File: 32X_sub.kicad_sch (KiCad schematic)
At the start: 103 parts, among them IC511 315-5684, IC512 315-5788, IC515 74HC74, IC516 74LS00, T520 TestPoint, T526 TestPoint, T527 TestPoint, T528 TestPoint, T547 TestPoint, T548 TestPoint, T555 TestPoint, T599 AS, X501 *3

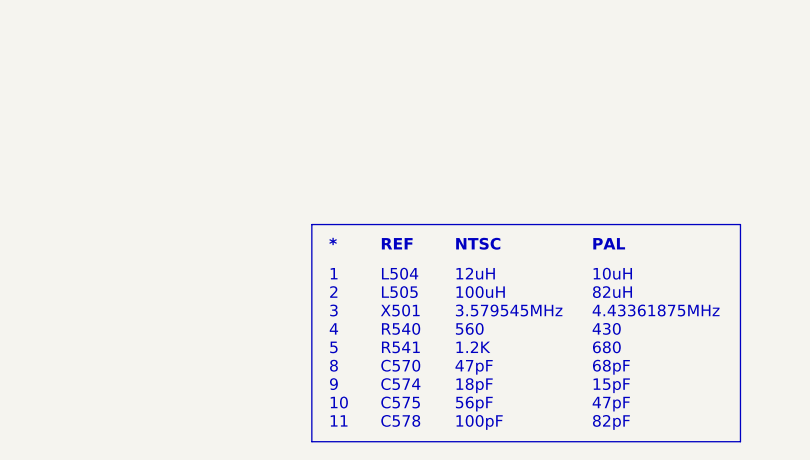
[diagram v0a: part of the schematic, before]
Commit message: Footprint improvements, general tidying.
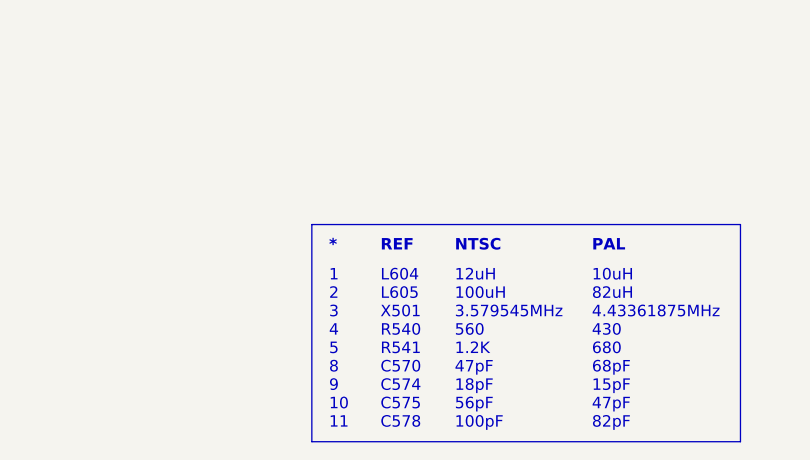
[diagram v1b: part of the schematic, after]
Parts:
- L501: footprint Inductor_SMD:L_1206_3216Metric -> Inductor_SMD:L_1210_3225Metric_Pad1.42x2.65mm_HandSolder
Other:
- note added: "L604 L605 X501 R540 R541 C570 C574 C575 C578"
- note removed: "L504 L505 X501 R540 R541 C570 C574 C575 C578"
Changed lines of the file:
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@@
     (effects (font (size 1.27 1.27) (thickness 0.254) bold) (justify left bottom))
   )
-  (text "L504\nL505\nX501\nR540\nR541\nC570\nC574\nC575\nC578" (at 257.175 278.13 0)
+  (text "L604\nL605\nX501\nR540\nR541\nC570\nC574\nC575\nC578" (at 257.175 278.13 0)
     (effects (font (size 1.27 1.27)) (justify left bottom))
   )
@@
       (effects (font (size 1.27 1.27)))
     )
-    (property "Footprint" "Inductor_SMD:L_1206_3216Metric" (at 346.075 60.96 0)
+    (property "Footprint" "Inductor_SMD:L_1210_3225Metric_Pad1.42x2.65mm_HandSolder" (at 346.075 60.96 0)
       (effects (font (size 1.27 1.27)) hide)
     )
@@
       (effects (font (size 1.27 1.27)))
     )
-    (property "Footprint" "Inductor_SMD:L_1206_3216Metric" (at 356.87 127 0)
+    (property "Footprint" "Inductor_SMD:L_1210_3225Metric_Pad1.42x2.65mm_HandSolder" (at 356.87 127 0)
       (effects (font (size 1.27 1.27)) hide)
     )
@@
       (effects (font (size 1.27 1.27)))
     )
-    (property "Footprint" "Inductor_SMD:L_1206_3216Metric" (at 357.505 88.9 0)
+    (property "Footprint" "Inductor_SMD:L_1210_3225Metric_Pad1.42x2.65mm_HandSolder" (at 357.505 88.9 0)
       (effects (font (size 1.27 1.27)) hide)
     )

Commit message: Added LCSC Part # for some of the bird seed
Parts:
- C554, C555: LCSC Part # (none) -> C2311750
- C556, C557: LCSC Part # (none) -> C2265986
- C558, C561, C562: LCSC Part # (none) -> C2250208
- C559, C560: LCSC Part # (none) -> C2264505
- C563, C564, C565, C566, C567, C568, C569, C580, C588, C589, C590, C591, C592, C593: LCSC Part # (none) -> C2237864
- C571: LCSC Part # (none) -> C2237165
- C573: LCSC Part # (none) -> C2236787
- C577, C579: LCSC Part # (none) -> C2179073
- C621: LCSC Part # (none) -> C1850591
- R45: LCSC Part # (none) -> C3988417
- R511, R512, R526, R527, R528, R529, R530, R531, R544: LCSC Part # (none) -> C313959
- R513, R515, R517, R519: LCSC Part # (none) -> C844640
- R514, R516, R539: LCSC Part # (none) -> C844841
- R518, R520, R549, R558, R621: LCSC Part # (none) -> C844937
- R521, R522: LCSC Part # (none) -> C844839
- R523: LCSC Part # (none) -> C2077067
- R524: LCSC Part # (none) -> C4311039
- R525: LCSC Part # (none) -> C3008897
- R532, R533, R534: LCSC Part # (none) -> C2090807
- R535, R536, R537: LCSC Part # (none) -> C2130183
- R547: LCSC Part # (none) -> C2078104
- R559: LCSC Part # (none) -> C2077049
- R560: LCSC Part # (none) -> C2088450
- R622: LCSC Part # (none) -> C844939

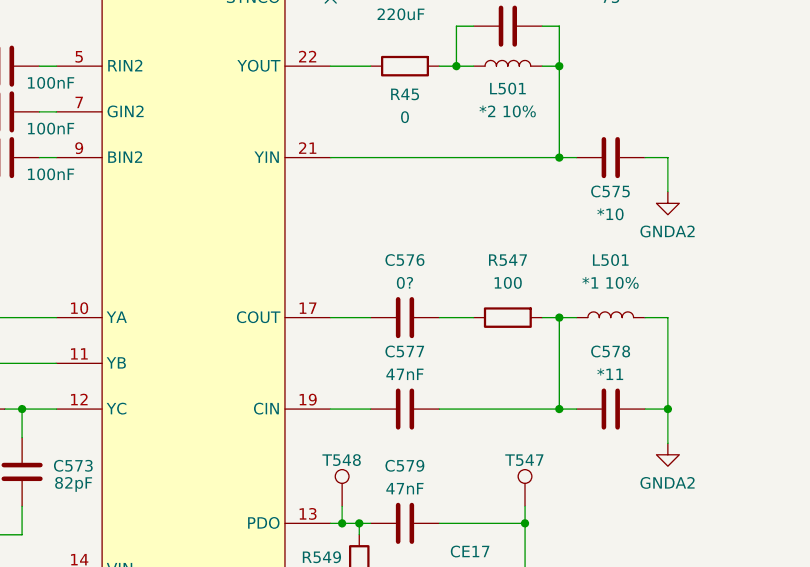
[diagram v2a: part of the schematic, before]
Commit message: Fix DRC warnings for graphics.
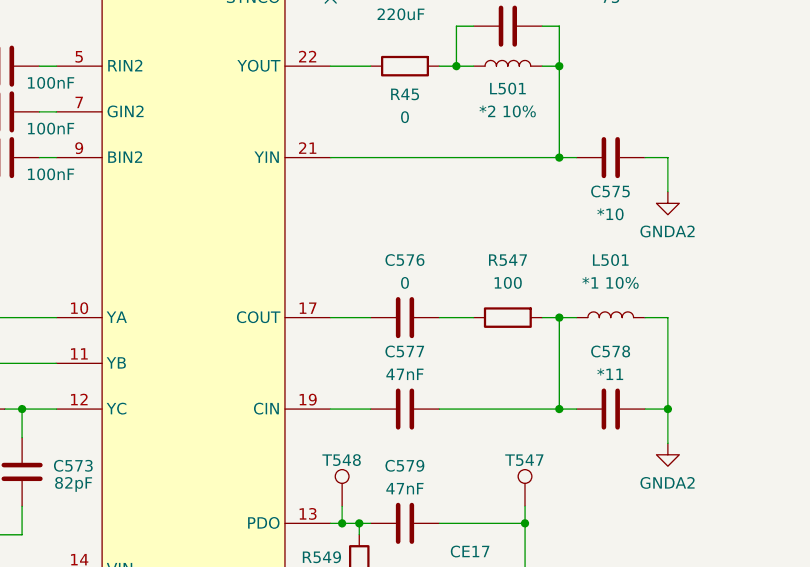
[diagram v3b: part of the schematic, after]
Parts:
- C576: value 0? -> 0
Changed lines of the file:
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@@
       (effects (font (size 1.27 1.27)))
     )
-    (property "Value" "0?" (at 334.645 85.09 90)
+    (property "Value" "0" (at 334.645 85.09 90)
       (effects (font (size 1.27 1.27)))
     )

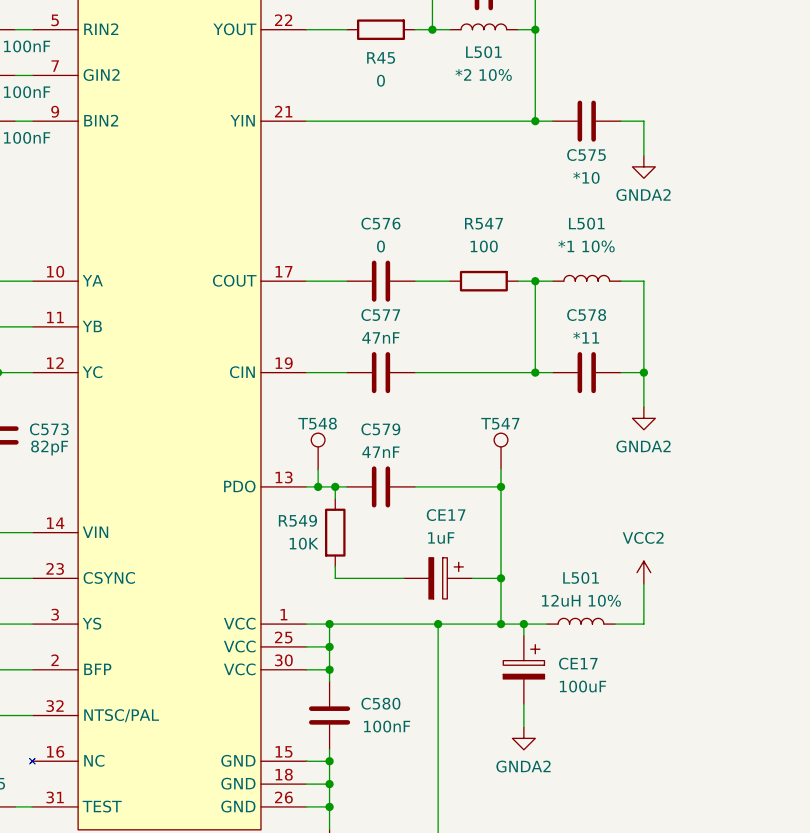
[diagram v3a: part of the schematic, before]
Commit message: Rev 1.1b
Bridged C576, not to be populated.

Fixing schematic ERC and update the PCB
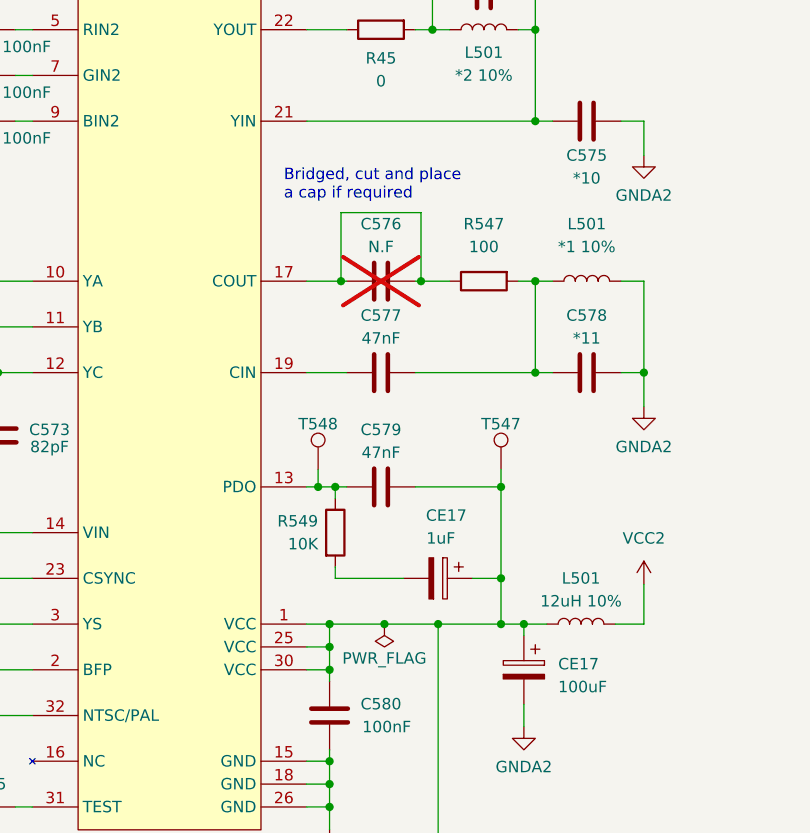
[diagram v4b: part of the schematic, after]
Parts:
- C576: value 0 -> N.F; now not fitted; now left out of the parts list
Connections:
- net at C576.2, R547.1: now also C576.1, IC512.17 (COUT)
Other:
- note added: "Bridged, cut and place a cap if required"
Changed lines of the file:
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@@
     (title "32X Sub")
     (date "2023-11-29")
-    (rev "1.1")
+    (rev "1.1b")
     (company "By Cosam")
     (comment 1 "Neptune")
@@
   (junction (at 186.055 254.635) (diameter 0) (color 0 0 0 0)
   )
+  (junction (at 335.026 127) (diameter 0) (color 0 0 0 0)
+  )
   (junction (at 328.93 129.54) (diameter 0) (color 0 0 0 0)
   )
@@
   (junction (at 183.515 200.66) (diameter 0) (color 0 0 0 0)
   )
+  (junction (at 339.09 88.9) (diameter 0) (color 0 0 0 0)
+  )
   (junction (at 169.545 101.6) (diameter 0) (color 0 0 0 0)
   )
@@
   (junction (at 233.68 127) (diameter 0) (color 0 0 0 0)
   )
+  (junction (at 330.2 88.9) (diameter 0) (color 0 0 0 0)
+  )
   (junction (at 314.325 221.615) (diameter 0) (color 0 0 0 0)
   )
@@
     (stroke (width 0) (type default))
   )
+  (wire (pts (xy 330.2 81.28) (xy 339.09 81.28))
+    (stroke (width 0) (type default))
+  )
   (wire (pts (xy 314.325 234.315) (xy 325.12 234.315))
     (stroke (width 0) (type default))
@@
     (stroke (width 0) (type default))
   )
+  (wire (pts (xy 330.2 88.9) (xy 330.835 88.9))
+    (stroke (width 0) (type default))
+  )
   (wire (pts (xy 351.79 56.515) (xy 351.79 60.96))
     (stroke (width 0) (type default))
@@
     (stroke (width 0) (type default))
   )
-  (wire (pts (xy 340.995 127) (xy 328.93 127))
+  (wire (pts (xy 340.995 127) (xy 335.026 127))
     (stroke (width 0) (type default))
   )
@@
     (stroke (width 0) (type default))
   )
+  (wire (pts (xy 339.09 81.28) (xy 339.09 88.9))
+    (stroke (width 0) (type default))
+  )
   (wire (pts (xy 227.33 214.63) (xy 231.775 214.63))
     (stroke (width 0) (type default))
@@
     (stroke (width 0) (type default))
   )
-  (wire (pts (xy 326.39 88.9) (xy 330.835 88.9))
+  (wire (pts (xy 326.39 88.9) (xy 330.2 88.9))
     (stroke (width 0) (type default))
   )
@@
     (stroke (width 0) (type default))
   )
-  (wire (pts (xy 338.455 88.9) (xy 342.265 88.9))
+  (wire (pts (xy 338.455 88.9) (xy 339.09 88.9))
     (stroke (width 0) (type default))
   )
@@
     (stroke (width 0) (type default))
   )
+  (wire (pts (xy 330.2 88.9) (xy 330.2 81.28))
+    (stroke (width 0) (type default))
+  )
   (wire (pts (xy 87.63 257.81) (xy 96.52 257.81))
     (stroke (width 0) (type default))
@@
     (stroke (width 0) (type default))
   )
+  (wire (pts (xy 335.026 127) (xy 328.93 127))
+    (stroke (width 0) (type default))
+  )
   (wire (pts (xy 112.395 209.55) (xy 112.395 219.71))
     (stroke (width 0) (type default))
@@
     (stroke (width 0) (type default))
   )
+  (wire (pts (xy 339.09 88.9) (xy 342.265 88.9))
+    (stroke (width 0) (type default))
+  )
   (wire (pts (xy 326.39 60.96) (xy 330.835 60.96))
     (stroke (width 0) (type default))
@@
     (effects (font (size 1.27 1.27) bold) (justify left bottom))
   )
+  (text "Bridged, cut and place\na cap if required" (at 323.85 80.01 0)
+    (effects (font (size 1.27 1.27)) (justify left bottom))
+  )
   (label "CTD4" (at 88.9 242.57 0) (fields_autoplaced)
     (effects (font (size 1.27 1.27)) (justify left bottom))
@@
     )
   )
+  (symbol (lib_id "power:PWR_FLAG") (at 335.026 127 180) (unit 1)
+    (in_bom yes) (on_board yes) (dnp no)
+    (property "Reference" "#FLG02" (at 335.026 128.905 0)
+      (effects (font (size 1.27 1.27)) hide)
+    )
+    (property "Value" "PWR_FLAG" (at 335.026 130.81 0)
+      (effects (font (size 1.27 1.27)))
+    )
+    (property "Footprint" "" (at 335.026 127 0)
+      (effects (font (size 1.27 1.27)) hide)
+    )
+    (property "Datasheet" "~" (at 335.026 127 0)
+      (effects (font (size 1.27 1.27)) hide)
+    )
+    (pin "1")
+    (instances
+      (project "Neptune"
+        (path "/bcc23b51-b742-4ae5-9dd6-d96a24058944/edde10e2-ce08-4180-9fbe-ab298dfbfa4c"
+          (reference "#FLG02") (unit 1)
+        )
+      )
+    )
+  )
   (symbol (lib_id "32X:315-5684") (at 119.38 30.48 0) (unit 1)
     (in_bom yes) (on_board yes) (dnp no) (fields_autoplaced)
@@
   )
   (symbol (lib_id "Device:C") (at 334.645 88.9 90) (unit 1)
-    (in_bom yes) (on_board yes) (dnp no)
+    (in_bom no) (on_board yes) (dnp yes)
     (property "Reference" "C576" (at 334.645 82.55 90)
       (effects (font (size 1.27 1.27)))
     )
-    (property "Value" "0" (at 334.645 85.09 90)
+    (property "Value" "N.F" (at 334.645 85.09 90)
       (effects (font (size 1.27 1.27)))
     )

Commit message: Added more JLC Part numbers
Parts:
- IC515: LCSC Part # (none) -> C3826856
- IC516: LCSC Part # (none) -> C140269
- L501: LCSC Part # (none) -> C394099
- L501: LCSC Part # (none) -> C394998
- L501: LCSC Part # (none) -> C75643
- TR501, TR502: LCSC Part # (none) -> C77991
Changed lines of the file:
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@@
       (effects (font (size 1.27 1.27)) hide)
     )
-    (property "LCSC Part #" "" (at 346.075 60.96 0)
+    (property "LCSC Part #" "C394099" (at 346.075 60.96 0)
       (effects (font (size 1.27 1.27)) hide)
     )
@@
       (effects (font (size 1.27 1.27)) hide)
     )
-    (property "LCSC Part #" "" (at 195.58 254.635 0)
+    (property "LCSC Part #" "C140269" (at 195.58 254.635 0)
       (effects (font (size 1.27 1.27)) hide)
     )
@@
       (effects (font (size 1.27 1.27)) hide)
     )
-    (property "LCSC Part #" "" (at 183.515 64.135 0)
+    (property "LCSC Part #" "C77991" (at 183.515 64.135 0)
       (effects (font (size 1.27 1.27)) hide)
     )
@@
       (effects (font (size 1.27 1.27)) hide)
     )
-    (property "LCSC Part #" "" (at 173.355 230.505 0)
+    (property "LCSC Part #" "C140269" (at 173.355 230.505 0)
       (effects (font (size 1.27 1.27)) hide)
     )
@@
       (effects (font (size 1.27 1.27)) hide)
     )
-    (property "LCSC Part #" "" (at 248.92 88.9 0)
+    (property "LCSC Part #" "C77991" (at 248.92 88.9 0)
       (effects (font (size 1.27 1.27)) hide)
     )
@@
       (effects (font (size 1.27 1.27)) hide)
     )
-    (property "LCSC Part #" "" (at 344.805 226.695 0)
+    (property "LCSC Part #" "C3826856" (at 344.805 226.695 0)
       (effects (font (size 1.27 1.27)) hide)
     )
@@
       (effects (font (size 1.27 1.27)) hide)
     )
-    (property "LCSC Part #" "" (at 356.87 127 0)
+    (property "LCSC Part #" "C394998" (at 356.87 127 0)
       (effects (font (size 1.27 1.27)) hide)
     )
@@
       (effects (font (size 1.27 1.27)) hide)
     )
-    (property "LCSC Part #" "" (at 374.65 226.695 0)
+    (property "LCSC Part #" "C140269" (at 374.65 226.695 0)
       (effects (font (size 1.27 1.27)) hide)
     )
@@
       (effects (font (size 1.27 1.27)) hide)
     )
-    (property "LCSC Part #" "" (at 183.515 209.55 0)
+    (property "LCSC Part #" "C3826856" (at 183.515 209.55 0)
       (effects (font (size 1.27 1.27)) hide)
     )
@@
       (effects (font (size 1.27 1.27)) hide)
     )
-    (property "LCSC Part #" "" (at 325.12 224.155 0)
+    (property "LCSC Part #" "C3826856" (at 325.12 224.155 0)
       (effects (font (size 1.27 1.27)) hide)
     )
@@
       (effects (font (size 1.27 1.27)) hide)
     )
-    (property "LCSC Part #" "" (at 195.58 230.505 0)
+    (property "LCSC Part #" "C140269" (at 195.58 230.505 0)
       (effects (font (size 1.27 1.27)) hide)
     )
@@
       (effects (font (size 1.27 1.27)) hide)
     )
-    (property "LCSC Part #" "" (at 357.505 88.9 0)
+    (property "LCSC Part #" "C75643" (at 357.505 88.9 0)
       (effects (font (size 1.27 1.27)) hide)
     )
@@
       (effects (font (size 1.27 1.27)) hide)
     )
-    (property "LCSC Part #" "" (at 219.71 214.63 0)
+    (property "LCSC Part #" "C140269" (at 219.71 214.63 0)
       (effects (font (size 1.27 1.27)) hide)
     )

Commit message: more component parts updated
Full in the * as PAL versions.
Added MPN for PCBWAY
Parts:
- C554, C555: MPN (none) -> VJ0805A332FXJTW1BC
- C556, C557: MPN (none) -> VJ0805A681FXJCW1BC
- C558, C561, C562: MPN (none) -> VJ0805A102FXJCW1BC
- C559, C560: MPN (none) -> VJ0805A222FXJCW1BC
- C563, C564, C565, C566, C567, C568, C569, C580, C588, C589, C590, C591, C592, C593: MPN (none) -> VJ0805Y104JXJMT
- C570: LCSC Part # (none) -> C162306; MPN (none) -> GRM21A5C2J680JWA1D
- C571: MPN (none) -> VJ0805A100FXJCW1BC
- C573: MPN (none) -> VJ0805A820FXJCW1BC
- C574: LCSC Part # (none) -> C726621; MPN (none) -> CC0805JRNPOCBN150
- C575: LCSC Part # (none) -> C437549; MPN (none) -> GRM21A5C2E470JW01D
- C577, C579: MPN (none) -> VJ0805Y473JXJCW1BC
- C578: LCSC Part # (none) -> C710971; MPN (none) -> GRM21A5C2E820JW01D
- C621: MPN (none) -> VJ0805Y105KXJTW1BC
- IC515: MPN (none) -> SN74HC74ANS
- IC516: MPN (none) -> SN74LS00NSR
- L501: MPN (none) -> FHW1210IF820JST
- L501: MPN (none) -> CMI322513X120KT
- L501: MPN (none) -> FHW1210IF100JST
- R45: MPN (none) -> RCG08050000Z0EA
- R511, R512, R526, R527, R528, R529, R530, R531, R544: MPN (none) -> CRCW080575R0FKEAHP
- R513, R515, R517, R519: MPN (none) -> CRCW08058K20FKEA
- R514, R516, R539: MPN (none) -> CRCW08053K00FKEA
- R518, R520, R549, R558, R621: MPN (none) -> CRCW080510K0FKEA
- R521, R522: MPN (none) -> CRCW0805330RFKEA
- R523: MPN (none) -> CRCW08054K70JNEAC
- R524: MPN (none) -> CRCW080510R0FKEB
- R525: MPN (none) -> CRCW08052K20JNEA
- R532, R533, R534: MPN (none) -> CRCW080533R0FKEAC
- R535, R536, R537: MPN (none) -> MCU08050C1600FPW00
- R540: LCSC Part # (none) -> C2081699; MPN (none) -> CRCW0805430RJNEA
- R541: LCSC Part # (none) -> C2085755; MPN (none) -> CRCW0805680RJNEA
- R547: MPN (none) -> CRCW0805100RJNEAHP
- R559: MPN (none) -> CRCW08052K00JNEA
- R560: MPN (none) -> TNPW080516K0BEEA
- R622: MPN (none) -> CRCW08051K00FKEA
- TR501, TR502: MPN (none) -> MMBT3904-TP
